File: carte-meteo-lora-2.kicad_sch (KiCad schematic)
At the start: 55 parts, among them J2 USB_C_Receptacle_USB2.0_14P, J4 Conn_01x04_Pin, J6 Conn_Coaxial, J7 Conn_Coaxial, J8 Conn_Coaxial, U3 HS96L03W2C03, U6 ESP32-C5, U8 SX1262TR8-GC, Y1 48M

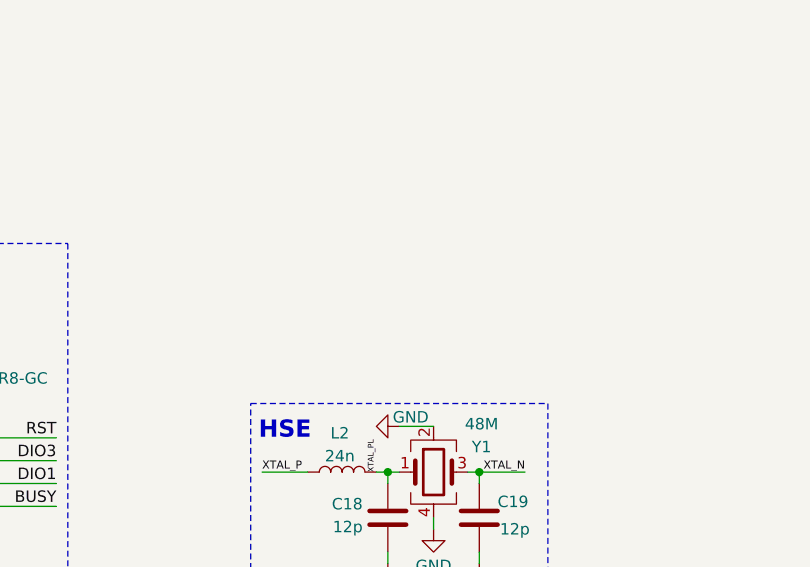
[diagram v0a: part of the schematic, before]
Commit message: schem: add boot/rst buttons
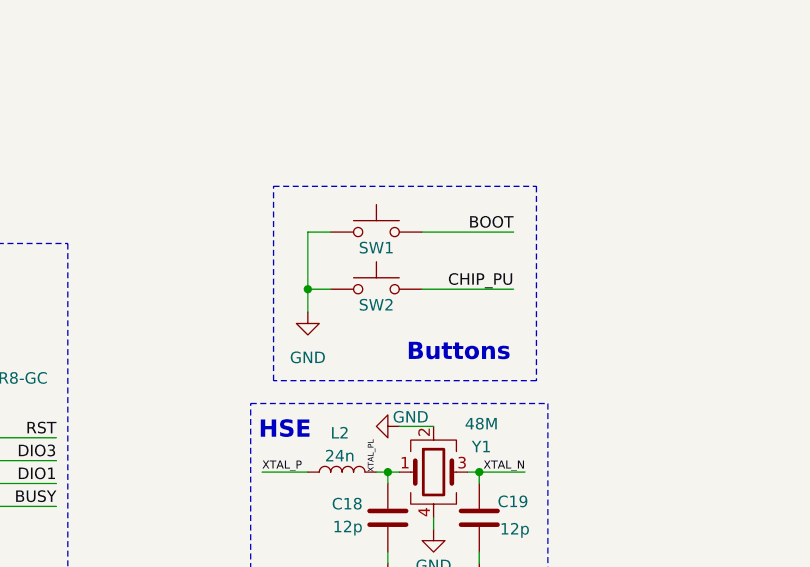
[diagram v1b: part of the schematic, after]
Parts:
- added SW1, SW2: SW_Push, Button_Switch_SMD:SW_SPST_TS-1088-xR020, symbol Switch:SW_Push
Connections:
- net BOOT: now also SW1.2
- net CHIP_PU: now also SW2.2
- net GND: now also SW1.1, SW2.1
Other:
- note added: "Buttons"

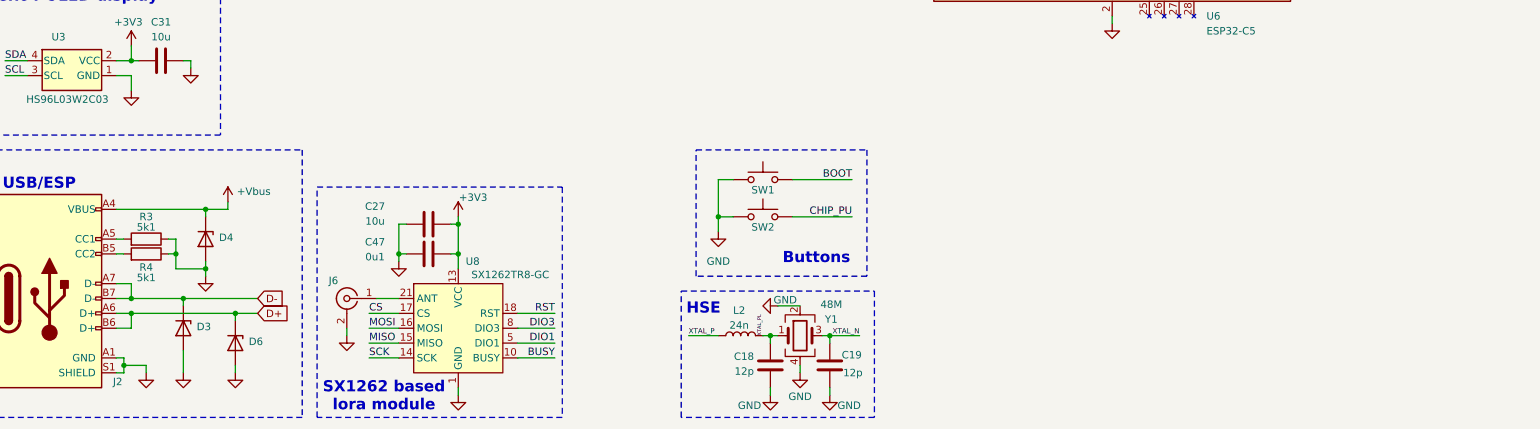
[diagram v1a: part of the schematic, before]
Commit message: schem: add LDL212 3V3 ldo
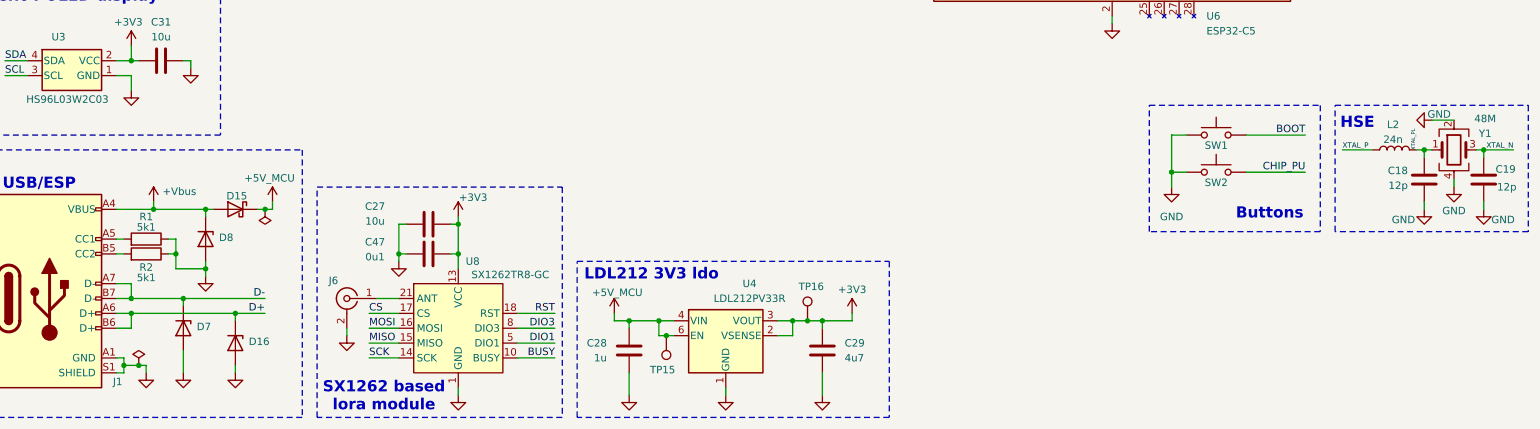
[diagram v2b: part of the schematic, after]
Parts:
- removed D3, D4, D6: H5VU10U, GLCS:Diode_DFN1006, symbol GLCS:H5VU10U
- removed J2: USB_C_Receptacle_USB2.0_14P, Connector_USB:USB_C_Receptacle_HRO_TYPE-C-31-M-12, symbol Connector:USB_C_Receptacle_USB2.0_14P
- removed R3, R4: 5k1, Resistor_SMD:R_0402_1005Metric, symbol Device:R
- added C28: 1u, Capacitor_SMD:C_0402_1005Metric, symbol Device:C
- added C29: 4u7, Capacitor_SMD:C_0402_1005Metric, symbol Device:C
- added D15: D_Schottky, Diode_SMD:D_SMA, symbol Device:D_Schottky
- added D16, D7, D8: H5VU10U, GLCS:Diode_DFN1006, symbol GLCS:H5VU10U
- added J1: USB_C_Receptacle_USB2.0_14P, Connector_USB:USB_C_Receptacle_HRO_TYPE-C-31-M-12, symbol Connector:USB_C_Receptacle_USB2.0_14P
- added R1, R2: 5k1, Resistor_SMD:R_0402_1005Metric, symbol Device:R
- added TP15, TP16: TestPoint, TestPoint:TestPoint_Pad_D2.0mm, symbol Connector:TestPoint
- added U4: LDL212PV33R, GLCS:DFN-6-1EP_2x2mm_P0.5mm_ST, symbol GLCS:LDL212PV33R
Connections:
- net +3V3: now also C29.1, TP16.1, U4.2 (VSENSE), U4.3 (VOUT)
- net +5V_MCU: now also C28.1, D15.1 (K), TP15.1, U4.4 (VIN), U4.6 (EN)
- net +Vbus: now also D15.2 (A), D8.1 (K), J1.A4 (VBUS), J1.A9 (VBUS), J1.B4 (VBUS), J1.B9 (VBUS)
- net D+: now also D16.1 (K), J1.A6 (D+), J1.B6 (D+)
- net D-: now also D7.1 (K), J1.A7 (D-), J1.B7 (D-)
- net GND: now also C28.2, C29.2, D16.2 (A), D7.2 (A), D8.2 (A), J1.A1 (GND), J1.A12 (GND), J1.B1 (GND), J1.B12 (GND), J1.S1 (SHIELD), R1.1, R2.1, U4.1 (GND)
- new net: J1.B5 (CC2), R2.2
- new net: J1.A5 (CC1), R1.2
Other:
- note added: "LDL212 3V3 ldo"
- moved on the sheet: C18, C19, L2, SW1, SW2, Y1

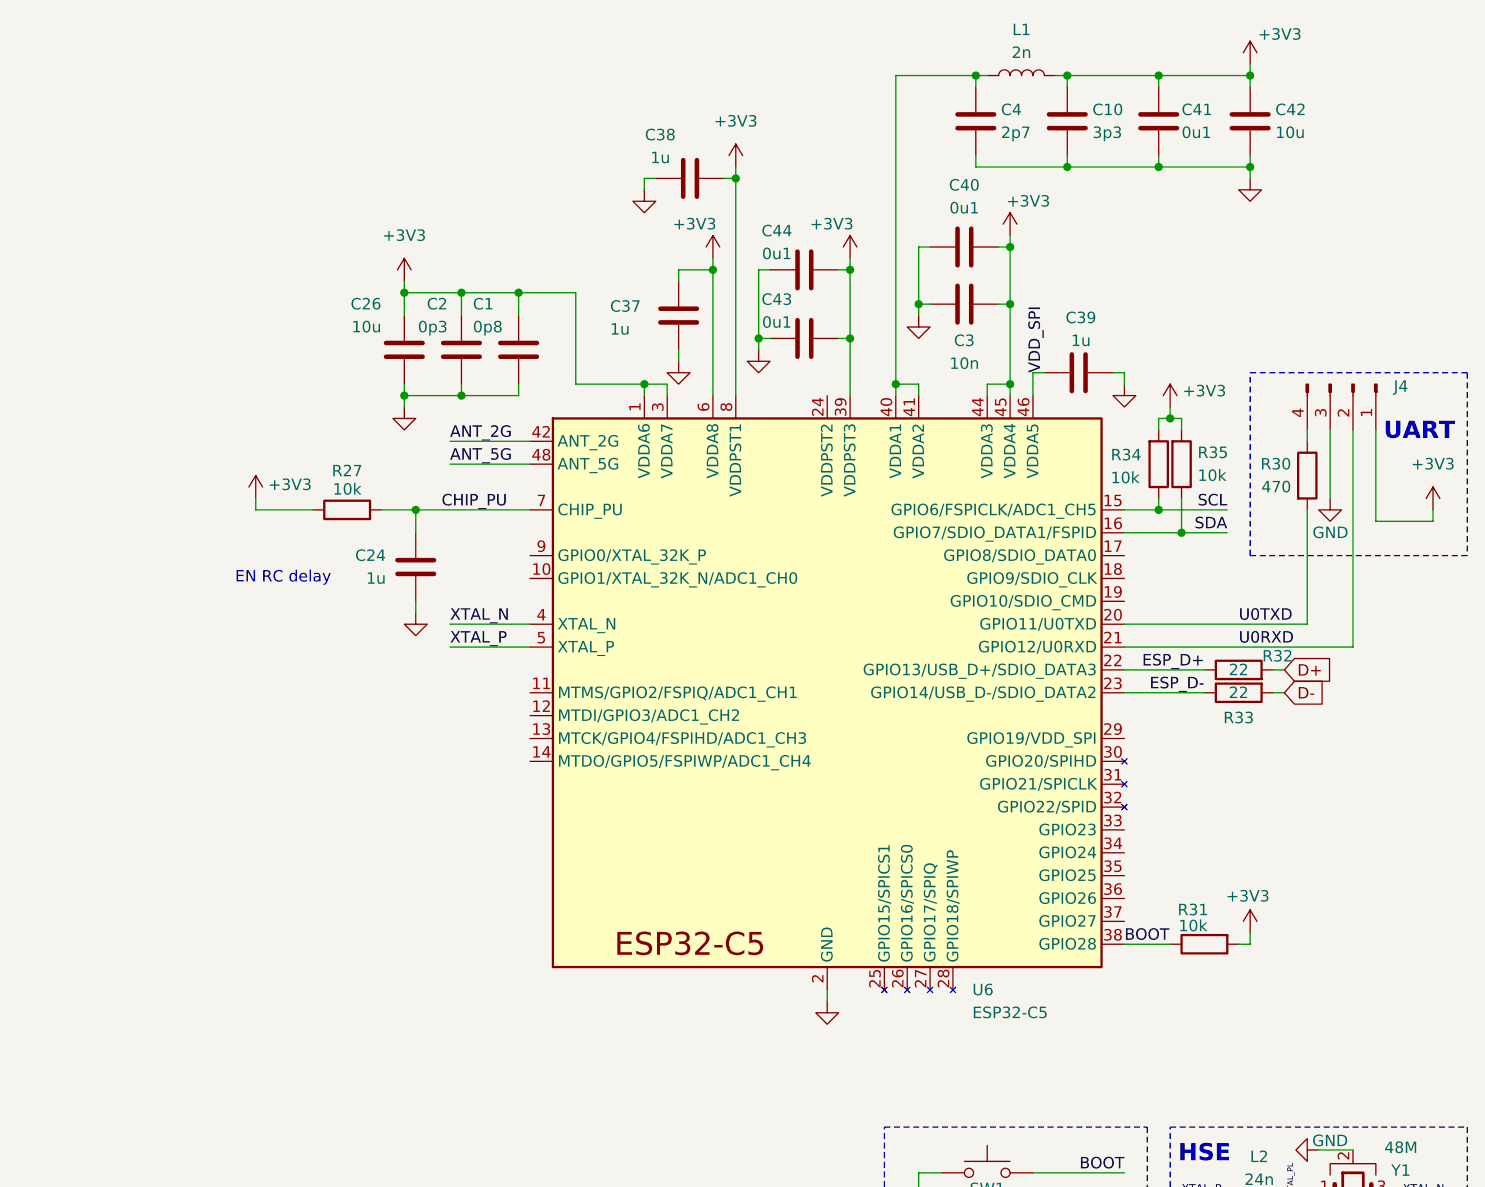
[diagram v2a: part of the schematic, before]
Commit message: schem: connect gpios to mcu
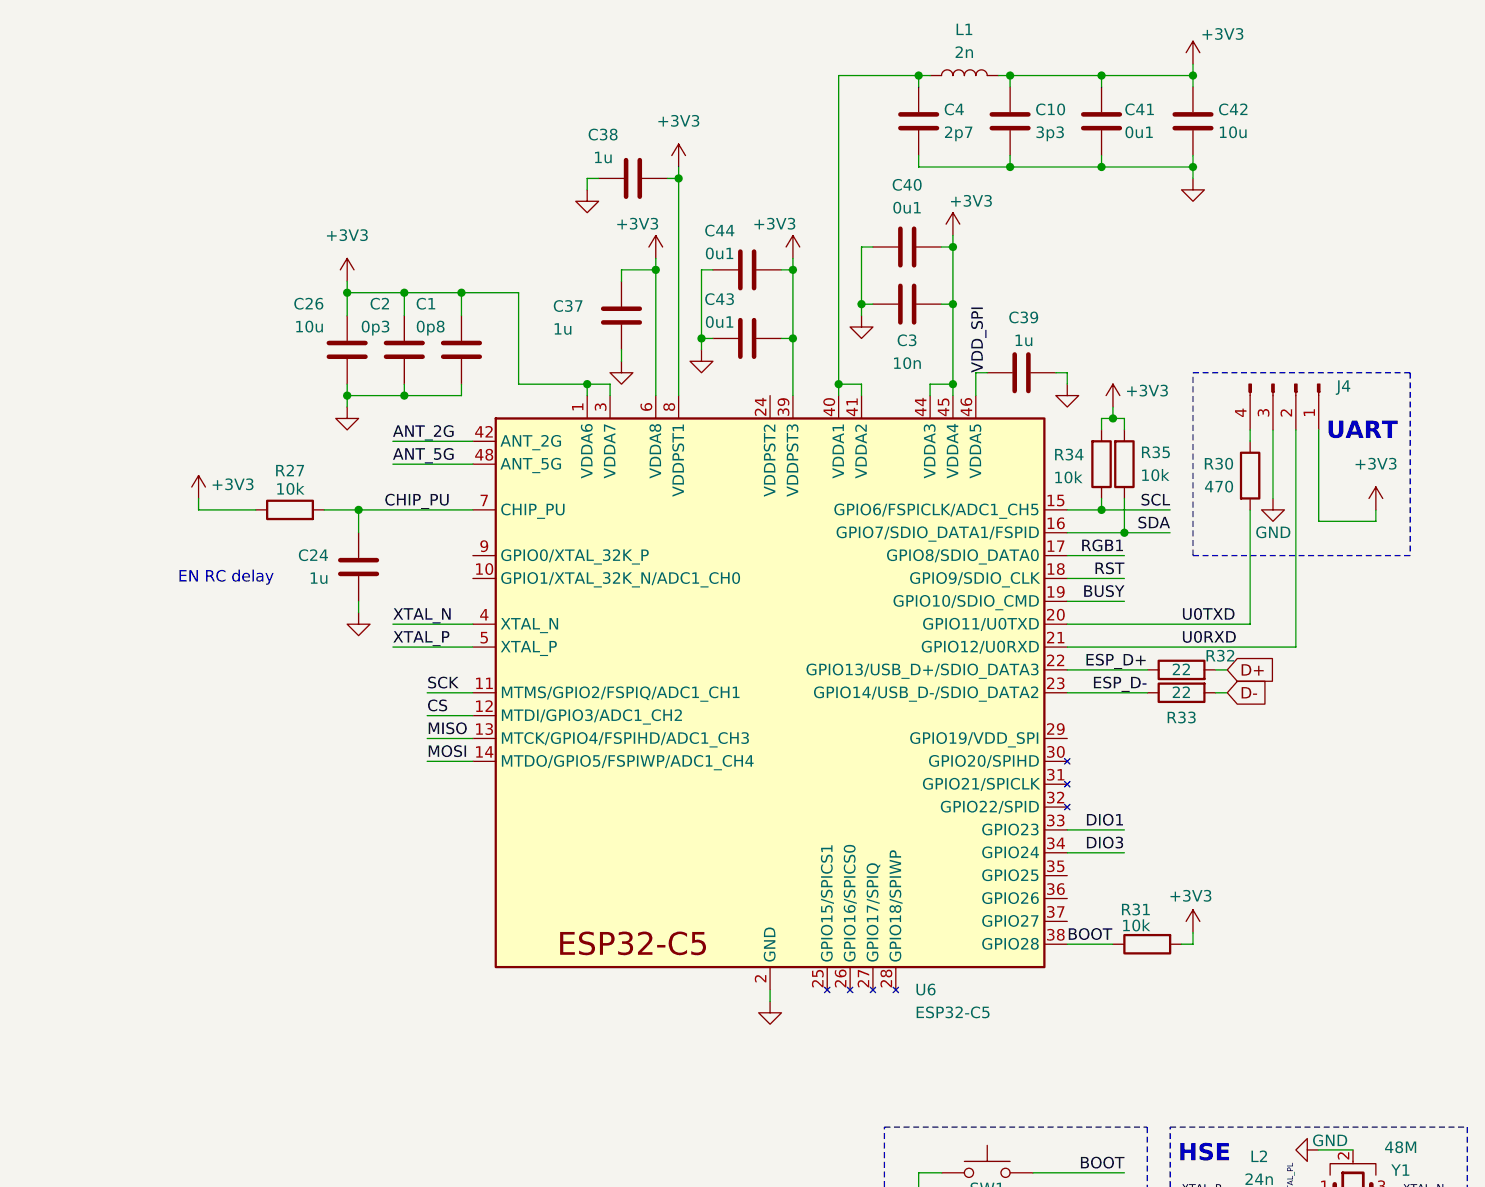
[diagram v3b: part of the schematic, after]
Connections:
- net BUSY: now also U6.19 (GPIO10/SDIO_CMD)
- net CS: now also U6.12 (MTDI/GPIO3/ADC1_CH2)
- net DIO1: now also U6.33 (GPIO23)
- net DIO3: now also U6.34 (GPIO24)
- net MISO: now also U6.13 (MTCK/GPIO4/FSPIHD/ADC1_CH3)
- net MOSI: now also U6.14 (MTDO/GPIO5/FSPIWP/ADC1_CH4)
- net RGB1: now also U6.17 (GPIO8/SDIO_DATA0)
- net RST: now also U6.18 (GPIO9/SDIO_CLK)
- net SCK: now also U6.11 (MTMS/GPIO2/FSPIQ/ADC1_CH1)
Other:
- moved on the sheet: C1, C10, C2, C24, C26, C3, C37, C38, C39, C4, C40, C41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

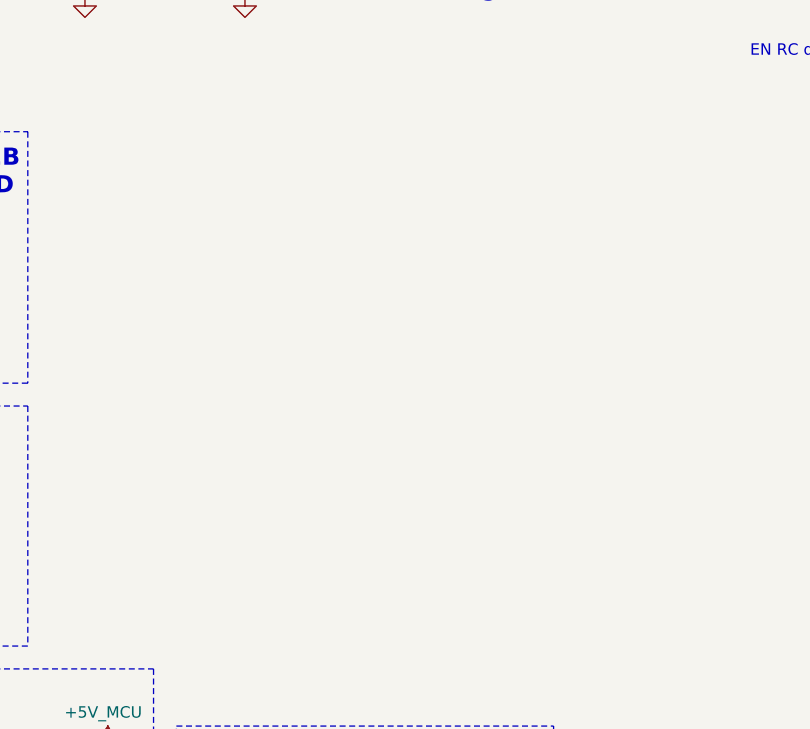
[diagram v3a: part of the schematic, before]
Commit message: schem: add cal kit
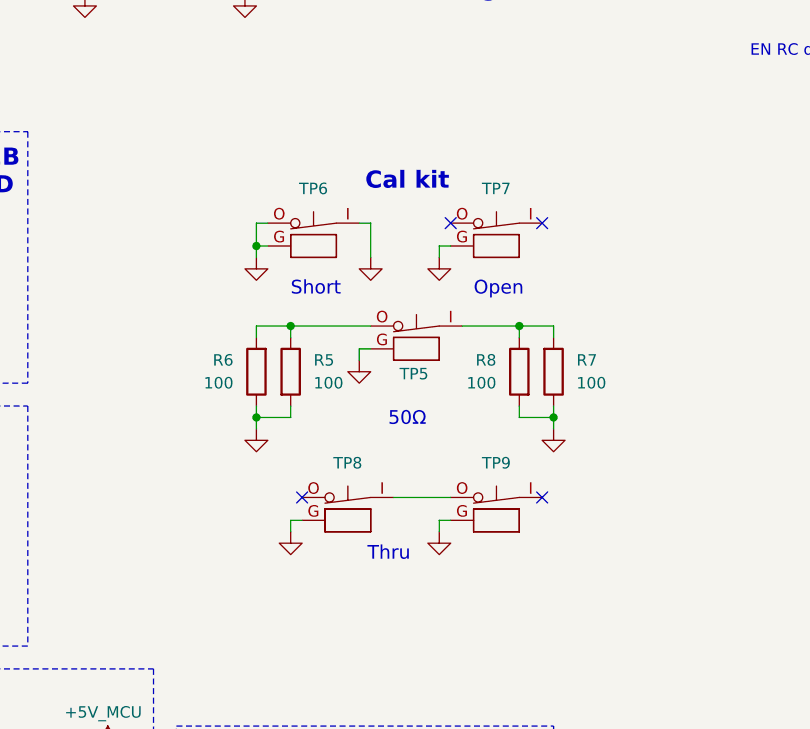
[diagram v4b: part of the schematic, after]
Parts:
- added R5, R6, R7, R8: 100, symbol Device:R
- added TP5, TP6, TP7, TP8, TP9: RF_switch_connector, symbol GLCS:RF_switch_connector
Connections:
- net GND: now also R5.2, R6.1, R7.1, R8.2, TP5.G, TP6.G, TP6.I, TP6.O, TP7.G, TP8.G, TP9.G
- new net: R7.2, R8.1, TP5.I
- new net: R5.1, R6.2, TP5.O
- new net: TP8.I, TP9.O
- no-connect marks 1 -> 5
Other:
- note added: "50Ω"
- note added: "Cal kit"
- note added: "Open"
- note added: "Short"
- note added: "Thru"
